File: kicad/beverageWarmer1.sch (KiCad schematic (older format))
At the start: 46 parts, among them J0 Conn_01x02, J1 Conn_01x02, U0 IRF7205TRPBF, U1 AD820ARMZ, U2 AD820ARMZ, U3 Op07DRZ, U4 Op07DRZ, U5 ADP1720, U6 TL750L10CD

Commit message: first push
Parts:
- removed C0, C1: 22u, Capacitor_SMD:C_1210_3225Metric_Pad1.33x2.70mm_HandSolder, symbol Device:C
- removed C100: 10n, Capacitor_SMD:C_0603_1608Metric_Pad1.08x0.95mm_HandSolder, symbol Device:C
- removed C500, C501, C600, C601: 1u, Capacitor_SMD:C_0603_1608Metric_Pad1.08x0.95mm_HandSolder, symbol Device:C
- removed D0: DIODE, Diode_SMD:D_SMC, symbol Device:D
- removed D400: D_Zener, Diode_SMD:D_SMC, symbol Device:D_Zener
- removed J0: Conn_01x02, Connector_PinHeader_2.54mm:PinHeader_1x02_P2.54mm_Vertical_SMD_Pin1Right, symbol Connector_Generic:Conn_01x02
- removed L0: 22u, customFootprints:MPXV1D1054, symbol Device:L
- removed R100, R101, R102, R103, R200, R300, R301, R302, R303, R305, R400: 1k, Resistor_SMD:R_0603_1608Metric_Pad0.98x0.95mm_HandSolder, symbol Device:R
- removed R201, R402: 10k, Resistor_SMD:R_0603_1608Metric_Pad0.98x0.95mm_HandSolder, symbol Device:R
- removed R304: 5.5k, Resistor_SMD:R_0603_1608Metric_Pad0.98x0.95mm_HandSolder, symbol Device:R
- removed R401, R404: 2k, Resistor_SMD:R_0603_1608Metric_Pad0.98x0.95mm_HandSolder, symbol Device:R
- removed R405: 0, Resistor_SMD:R_0603_1608Metric_Pad0.98x0.95mm_HandSolder, symbol Device:R
- removed TH400, TH401: Thermistor, Resistor_THT:R_Axial_DIN0204_L3.6mm_D1.6mm_P2.54mm_Vertical, symbol Device:Thermistor
- removed TP0, TP1, TP100, TP2, TP300, TP400, TP401, TP402: TestPoint, TestPoint:TestPoint_Pad_D2.5mm, symbol Connector:TestPoint
- removed U0: IRF7205TRPBF, Package_SO:SOIC-8_3.9x4.9mm_P1.27mm, symbol customSymbols:IRF7205TRPBF
- removed U1, U2: AD820ARMZ, Package_SO:MSOP-8_3x3mm_P0.65mm, symbol customSymbols:AD820ARMZ
- removed U4: Op07DRZ, Package_SO:SOIC-8_3.9x4.9mm_P1.27mm, symbol customSymbols:Op07D
- removed U5: ADP1720, Package_SO:MSOP-8_3x3mm_P0.65mm, symbol customSymbols:ADP1720
- removed U6: TL750L10CD, Package_SO:SOIC-8_3.9x4.9mm_P1.27mm, symbol customSymbols:TL750L10CD
- added C1, C15, C16, C17, C5, C6, C7, C8, C9: 1u, Capacitor_SMD:C_0603_1608Metric, symbol Device:C_Small
- added C10, C11, C12, C13, C14, C18, C2, C3: 0.1u, Capacitor_SMD:C_0603_1608Metric, symbol Device:C_Small
- added C4: 10u, Capacitor_SMD:C_0603_1608Metric, symbol Device:C_Small
- added D1: D, symbol Device:D_Small
- added D2: 5.6V, symbol Device:D_Zener_Small
- added D3: RED, symbol Device:LED_Small
- added D4: GREEN, symbol Device:LED_Small
- added D5, D6: V3FL45, Diode_SMD:D_SMF, symbol Device:D_Small
- added F1: 3A, Fuse:Fuse_0603_1608Metric, symbol Device:Fuse_Small
- added FB1: FB, symbol Device:Ferrite_Bead_Small
- added J2: CAN_CONN, Connector_Molex:Molex_Micro-Fit_3.0_43650-0200_1x02_P3.00mm_Horizontal, symbol Connector_Generic:Conn_01x02
- added J3: SWD, Connector_PinSocket_1.27mm:PinSocket_2x03_P1.27mm_Vertical, symbol Connector_Generic:Conn_02x03_Odd_Even
- added J4: THERM_CONN, Connector_Molex:Molex_Micro-Fit_3.0_43650-0200_1x02_P3.00mm_Horizontal, symbol Connector_Generic:Conn_01x02
- added L1: 68uH, Inductor_SMD:L_Bourns_SRR1260, symbol Device:L_Small
- added Q1, Q4: Q_PMOS_DGS, customFootprints:SISS05DN-T1-GE3, symbol Device:Q_PMOS_DGS
- added Q2: Q_PMOS_GDS, Package_TO_SOT_SMD:SOT-23, symbol Device:Q_PMOS_GDS
- added Q3: Q_NMOS_GSD, Package_TO_SOT_SMD:SOT-23, symbol Device:Q_NMOS_GSD
- added R1, R11, R12, R14, R15, R16, R27, R29, R3, R4, R5, R6, R7, R8, R9: 1k, symbol Device:R_Small
- added R10, R17, R18: 2, symbol Device:R_Small
- added R13: 120, symbol Device:R_Small
- added R19, R22, R23, R24, R26: 0, symbol Device:R_Small
- added R2, R28: 3k, symbol Device:R_Small
- added R20: 2k, symbol Device:R_Small
- added R21: 10k, symbol Device:R_Small
- added R25: 5, symbol Device:R_Small
- added R30, R31, R32, R33, R34, R35: 1, customFootprints:4320_SMD_RES, symbol Device:R
- added SW1: RESET, Button_Switch_SMD:SW_SPST_B3U-1000P, symbol Switch:SW_SPST
- added SW2: USER, Button_Switch_SMD:SW_SPST_B3U-1000P, symbol Switch:SW_SPST
- added U1: STM32F103TBUx, Package_DFN_QFN:QFN-36-1EP_6x6mm_P0.5mm_EP4.1x4.1mm, symbol MCU_ST_STM32F1:STM32F103TBUx
- added U2: MIC5283-3.3ML-TR, Package_DFN_QFN:DFN-8-1EP_3x3mm_P0.65mm_EP1.55x2.4mm, symbol chum-bucket:MIC5283-3.3ML-TR
- added U4: TL391B, Package_TO_SOT_SMD:SOT-23-5, symbol beverageWarmer1-rescue:TL391B
- added U5: SN65HVD232, Package_SO:SOIC-8_3.9x4.9mm_P1.27mm, symbol Interface_CAN_LIN:SN65HVD232
- J1: value Conn_01x02 -> POWER; footprint Connector_PinHeader_2.54mm:PinHeader_1x02_P2.54mm_Vertical_SMD_Pin1Right -> Connector_Molex:Molex_Micro-Fit_3.0_43650-0200_1x02_P3.00mm_Horizontal; Digi (none) -> WM1860-ND; Digikey S1013E-02-ND -> (none)
- U3: symbol customSymbols:Op07D -> beverageWarmer1-rescue:Op07D-customSymbols; Have (none) -> Yes
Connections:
- net labels added: +3.3VA, +3V3, ANALOG_SPARE_1, ANALOG_SPARE_2, ANALOG_SPARE_3, BATT_VOLTAGE_AI, BATT_VOLTAGE_FILT, BUCK_OUTPUT_AI, BUCK_OUTPUT_FILT, BUCK_PWM, CAN_N, CAN_P, CAN_UART_N, CAN_UART_P, LED_1, LED_2, PWM_SPARE_1, PWM_SPARE_2, SWCLK, SWDIO, THERM_OUTPUT_FILT_AI, THERM_OUTPUT_UNFILT_AI, USER_SW, ~SW_RESET
- net labels removed: +10V, +5V, PWM_OUT
- wire segments 157 -> 235
- no-connect marks 4 -> 6
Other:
- note added: "A 25W, STM32 based, PID controlled beverage warmer. \n"
- note added: "CAN_UART_P = TX data\nCAN_UART_N = RX data\nLayout note: route all data lines as 60 ohm trace"
- note added: "Digital/MCU"
- note added: "Layout note: place decoupling capacitors as \nclose to mcu 3v3 and gndpins as possible."
- note added: "Power Input"
- note added: "Power Stage/Heating"
- note added: "Project: Wood Stove\n"
- note added: "TO DO: Pick corner frequency for filter\n"
- note added: "TO DO: SIM THIS\n"
- note added: "Thermistor Interface"
- note added: "Undervoltage, overcurrent and reverse voltage protection."
- note removed: "DNC"

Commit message: 2nd commit
changed gate drive for buck converter
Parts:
- removed Q2: Q_PMOS_GDS, Package_TO_SOT_SMD:SOT-23, symbol Device:Q_PMOS_GDS
- removed Q3: Q_NMOS_GSD, Package_TO_SOT_SMD:SOT-23, symbol Device:Q_NMOS_GSD
- added C19, C20: 0.1u, Capacitor_SMD:C_0603_1608Metric, symbol Device:C_Small
- added TP1: ANA_SPARE_1, symbol Connector:TestPoint
- added TP2: ANA_SPARE_2, symbol Connector:TestPoint
- added TP3: PWM_SPARE_1, symbol Connector:TestPoint
- added TP4: PWM_SPARE_2, symbol Connector:TestPoint
- added U6: MCP1402T-E, Package_TO_SOT_SMD:SOT-23-5, symbol beverageWarmer1-rescue:MCP1402T-E
- C12, C13: Voltage 16V -> 6.3v
- D1: value D -> V3FL45; footprint (none) -> Diode_SMD:D_SMF; Digi (none) -> V3FL45HM3/HGICT-ND
- D2: footprint (none) -> Diode_SMD:D_SOD-123; Digi (none) -> DDZ5V6BDICT-ND
- D3: footprint (none) -> LED_SMD:LED_0603_1608Metric; Digi (none) -> 754-1123-1-ND
- D4: footprint (none) -> LED_SMD:LED_0603_1608Metric; Digi (none) -> 754-1357-1-ND
- FB1: footprint (none) -> Inductor_SMD:L_0603_1608Metric; Digi (none) -> 490-1015-1-ND
- R17, R18: value 2 -> 1k
- R19: value 0 -> 1k
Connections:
- net labels added: ANALOG_SPARE_1_FILT, ANALOG_SPARE_2_FILT
- net labels removed: ANALOG_SPARE_3
- wire segments 235 -> 240
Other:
- note added: "TO DO: \n- Add digi P/N for connector pre-crimped leads\n- Add digi P/N for thermistor \n- Add digi P/N for Thermal interface material\n- Add digi P/N for CAN to UART adapter?"

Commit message: Final Sch Push?
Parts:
- C1, C15, C16: Digi (none) -> 445-6931-1-ND
- C10, C11, C14, C18, C2, C3: Digi (none) -> 1276-1019-1-ND
- C12, C13, C20: Digi (none) -> 1276-1019-1-ND; Voltage 6.3v -> 16V
- C17: value 1u -> 0.1u; Digi (none) -> 1276-1019-1-ND; Voltage 6.3V -> 16V
- C19: value 0.1u -> 1u; Digi (none) -> 445-6931-1-ND; Voltage 6.3v -> 16V
- C4: footprint Capacitor_SMD:C_0603_1608Metric -> Capacitor_SMD:C_1206_3216Metric; Digi (none) -> 1276-6641-1-ND
- R1, R11, R12, R14, R15, R16, R17, R18, R27, R4, R5, R6, R7: footprint (none) -> Resistor_SMD:R_0603_1608Metric; Digi (none) -> RMCF0603JJ1K00CT-ND
- R10: value 2 -> 10; footprint (none) -> Resistor_SMD:R_0603_1608Metric; Digi (none) -> A130079CT-ND
- R13: footprint (none) -> Resistor_SMD:R_0603_1608Metric; Digi (none) -> A129677CT-ND
- R19: value 1k -> 3k; footprint (none) -> Resistor_SMD:R_0603_1608Metric; Digi (none) -> RMCF0603FT3K00CT-ND; Tolerance (none) -> 1%
- R2, R28: footprint (none) -> Resistor_SMD:R_0603_1608Metric; Digi (none) -> RMCF0603FT3K00CT-ND; Tolerance (none) -> 1%
- R20: value 2k -> 1k; footprint (none) -> Resistor_SMD:R_0603_1608Metric; Digi (none) -> RMCF0603JJ1K00CT-ND
- R21, R29, R3: footprint (none) -> Resistor_SMD:R_0603_1608Metric; Digi (none) -> RMCF0603FT1K00CT-ND; Tolerance (none) -> 1%
- R22, R23, R24, R26: footprint (none) -> Resistor_SMD:R_0603_1608Metric; Digi (none) -> 2019-RK73Z1JTTDCT-ND
- R25: value 5 -> 10; footprint (none) -> Resistor_SMD:R_0603_1608Metric; Digi (none) -> A130079CT-ND
- R31: Digi (none) -> A143800CT-ND; Digikey A143800CT-ND -> (none)
- R8: value 1k -> 270; footprint (none) -> Resistor_SMD:R_0805_2012Metric; Digi (none) -> A130470CT-ND; Power (none) -> 1/4W
- R9: value 1k -> 30; footprint (none) -> Resistor_SMD:R_0805_2012Metric; Digi (none) -> 2019-RK73H2ATTD30R0FCT-ND; Power (none) -> 1/4W
- TP1, TP2, TP3, TP4: footprint (none) -> TestPoint:TestPoint_Pad_D1.0mm
- U1: value STM32F103TBUx -> STM32F103TBU
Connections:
- no-connect marks 6 -> 14
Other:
- note added: "1591 Hz corner frequency. This is ok."
- note added: "1591 Hz corner frequency. \n"
- note added: "Brightness set for 50mcd\n"
- note added: "TO DO: \n- Add digi P/N for connector pre-crimped leads\n- Add digi P/N for thermistor \n- Add digi P/N for passives \n- Add digi P/N for Thermal interface material\n- Add digi P/N for CAN to UART adapter?"
- note removed: "TO DO: Pick corner frequency for filter\n"
- note removed: "TO DO: \n- Add digi P/N for connector pre-crimped leads\n- Add digi P/N for thermistor \n- Add digi P/N for Thermal interface material\n- Add digi P/N for CAN to UART adapter?"

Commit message: Preliminary Layout Complete
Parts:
- C1, C10, C11, C12, C13, C14, C15, C16, C17, C18, C19, C2, C20, C3, C4, C5, C6, C7, C8, C9: symbol Device:C_Small -> beverageWarmer1-rescue:C_Small-Device
- D1, D5, D6: symbol Device:D_Small -> beverageWarmer1-rescue:D_Small-Device
- D2: symbol Device:D_Zener_Small -> beverageWarmer1-rescue:D_Zener_Small-Device
- D3, D4: symbol Device:LED_Small -> beverageWarmer1-rescue:LED_Small-Device
- F1: symbol Device:Fuse_Small -> beverageWarmer1-rescue:Fuse_Small-Device
- FB1: symbol Device:Ferrite_Bead_Small -> beverageWarmer1-rescue:Ferrite_Bead_Small-Device
- J1, J2, J4: symbol Connector_Generic:Conn_01x02 -> beverageWarmer1-rescue:Conn_01x02-Connector_Generic
- J3: symbol Connector_Generic:Conn_02x03_Odd_Even -> beverageWarmer1-rescue:Conn_02x03_Odd_Even-Connector_Generic
- L1: symbol Device:L_Small -> beverageWarmer1-rescue:L_Small-Device
- Q1, Q4: symbol Device:Q_PMOS_DGS -> beverageWarmer1-rescue:Q_PMOS_DGS-Device
- R1, R10, R11, R12, R13, R14, R15, R16, R17, R18, R19, R2, R20, R21, R22, R23, R24, R25, R26, R27, R28, R29, R3, R4, R5, R6, R7, R8, R9: symbol Device:R_Small -> beverageWarmer1-rescue:R_Small-Device
- R30, R31, R32, R33, R34, R35: symbol Device:R -> beverageWarmer1-rescue:R-Device
- SW1, SW2: symbol Switch:SW_SPST -> beverageWarmer1-rescue:SW_SPST-Switch
- TP1, TP2, TP3, TP4: symbol Connector:TestPoint -> beverageWarmer1-rescue:TestPoint-Connector
- U1: symbol MCU_ST_STM32F1:STM32F103TBUx -> beverageWarmer1-rescue:STM32F103TBUx-MCU_ST_STM32F1
- U2: symbol chum-bucket:MIC5283-3.3ML-TR -> beverageWarmer1-rescue:MIC5283-3.3ML-TR-chum-bucket
- U5: symbol Interface_CAN_LIN:SN65HVD232 -> beverageWarmer1-rescue:SN65HVD232-Interface_CAN_LIN
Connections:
- wire segments 240 -> 244

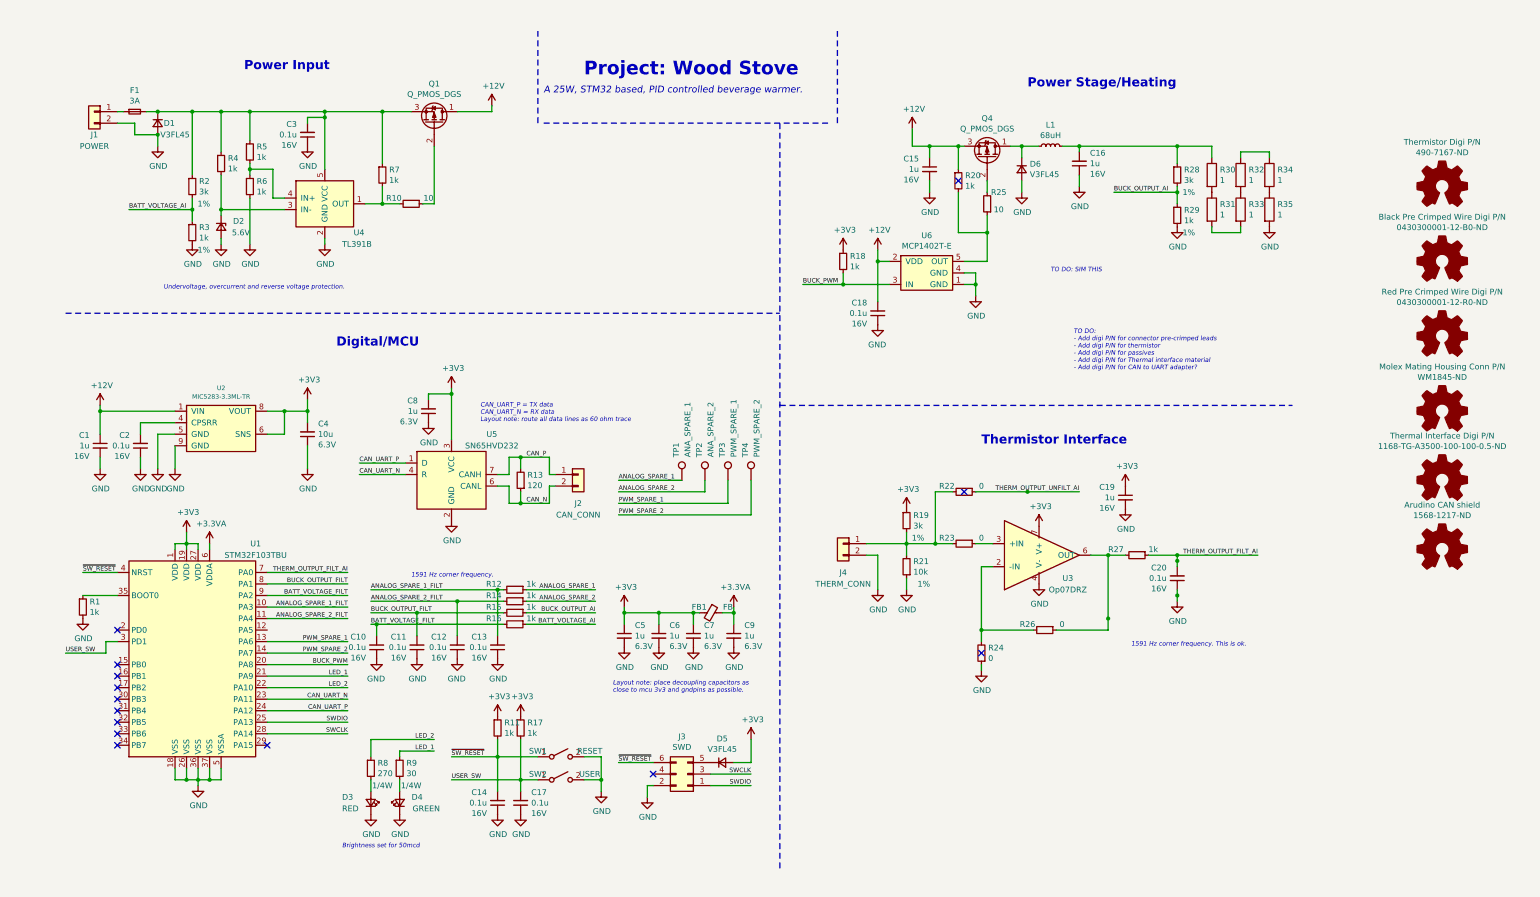
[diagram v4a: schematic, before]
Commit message: small ss and copper changes
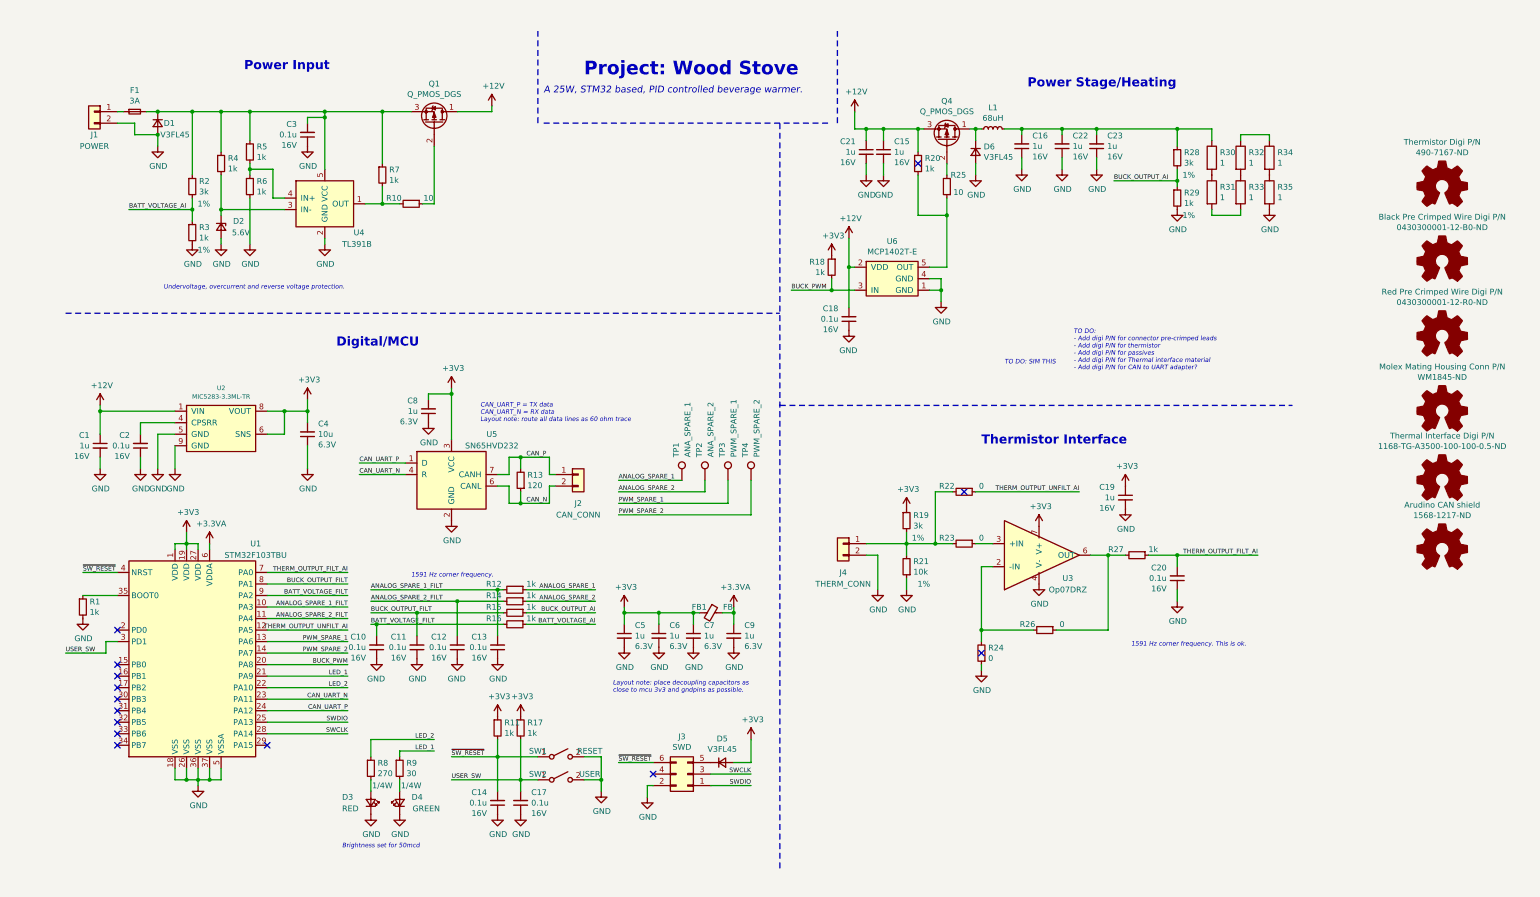
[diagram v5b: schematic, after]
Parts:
- added C21, C22, C23: 1u, Capacitor_SMD:C_0603_1608Metric, symbol beverageWarmer1-rescue:C_Small-Device
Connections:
- net +12V: now also C21.1
- net GND: now also C21.2, C22.1, C23.1
- net THERM_OUTPUT_UNFILT_AI: now also U1.12 (PA5)
- net at C16.2, L1.2, R28.1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: now also C22.2, C23.2
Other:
- moved on the sheet: C15, C16, C18, D6, L1, Q4, R18, R20, R25, R28, R29, R30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

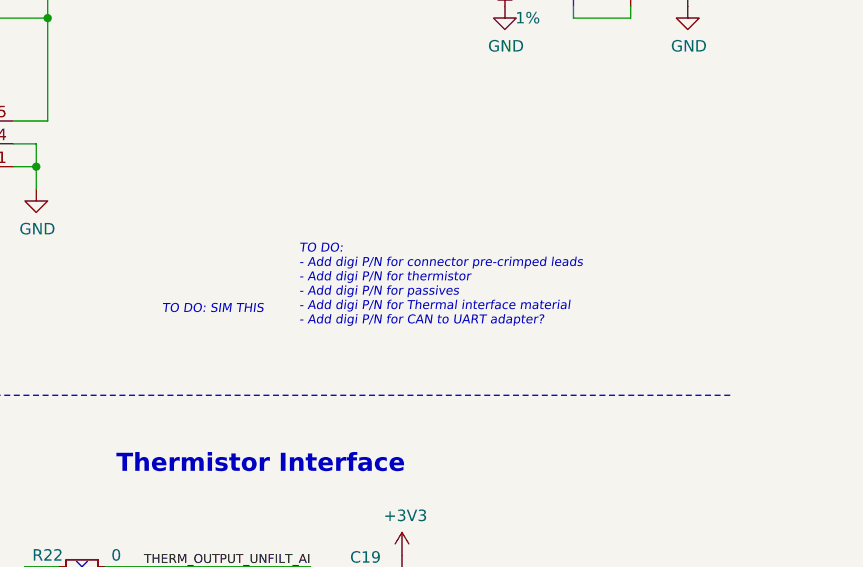
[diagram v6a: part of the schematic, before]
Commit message: firstTryPWM
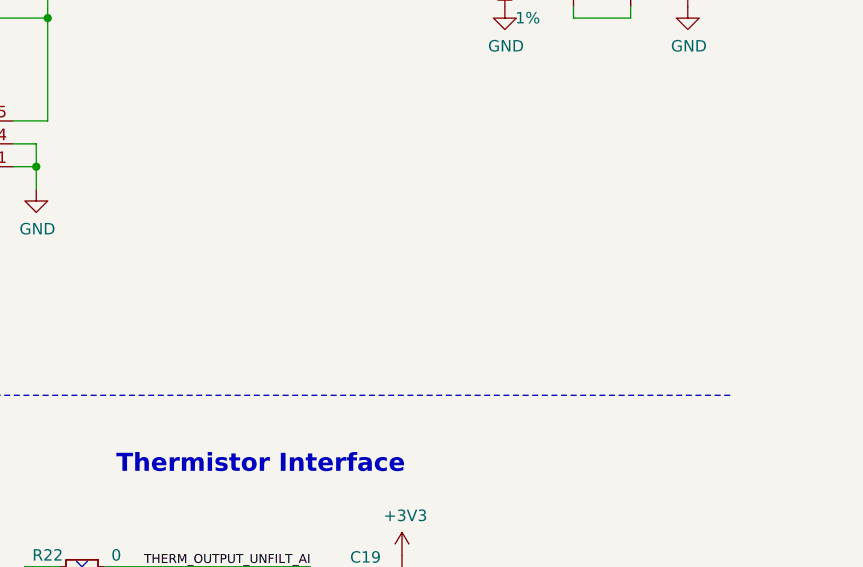
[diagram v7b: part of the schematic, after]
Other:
- note removed: "TO DO: SIM THIS\n"
- note removed: "TO DO: \n- Add digi P/N for connector pre-crimped leads\n- Add digi P/N for thermistor \n- Add digi P/N for passives \n- Add digi P/N for Thermal interface material\n- Add digi P/N for CAN to UART adapter?"
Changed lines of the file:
@@
 Text Label 3850 6800 0    39   ~ 0
 ~SW_RESET
-Text Notes 8650 3400 0    39   Italic 0
-TO DO: SIM THIS\n
 Wire Wire Line
 	8150 1650 8150 1750
@@
 Wire Wire Line
 	5300 4700 6450 4700
-Text Notes 9250 3450 0    39   Italic 0
-TO DO: \n- Add digi P/N for connector pre-crimped leads\n- Add digi P/N for thermistor \n- Add digi P/N for passives \n- Add digi P/N for Thermal interface material\n- Add digi P/N for CAN to UART adapter?
 $Comp
 L beverageWarmer1-rescue:Logo_Open_Hardware_Small-Graphic #LOGO1
